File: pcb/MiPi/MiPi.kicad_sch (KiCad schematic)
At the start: 35 parts, among them J3 USB_C_Receptacle_USB2.0_14P, SW1 SW_Push, SW2 SW_Push, U1 RP2350_60QFN, U6 NCP1117-3.3_SOT223, Y1 Crystal_GND24

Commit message: Routed the analog switch and audio amp and audio jack
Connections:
- net REG_VIN is gone; now on net +5V: C38.1, U6.3 (VI)
- net GP20: now reaches U1.32 (GPIO20)
- net GP21: now reaches U1.33 (GPIO21)
- net GP22: now reaches U1.34 (GPIO22)
- net GP23: now reaches U1.35 (GPIO23)
- net GP24: now reaches U1.36 (GPIO24)
- net GP25: now reaches U1.37 (GPIO25)

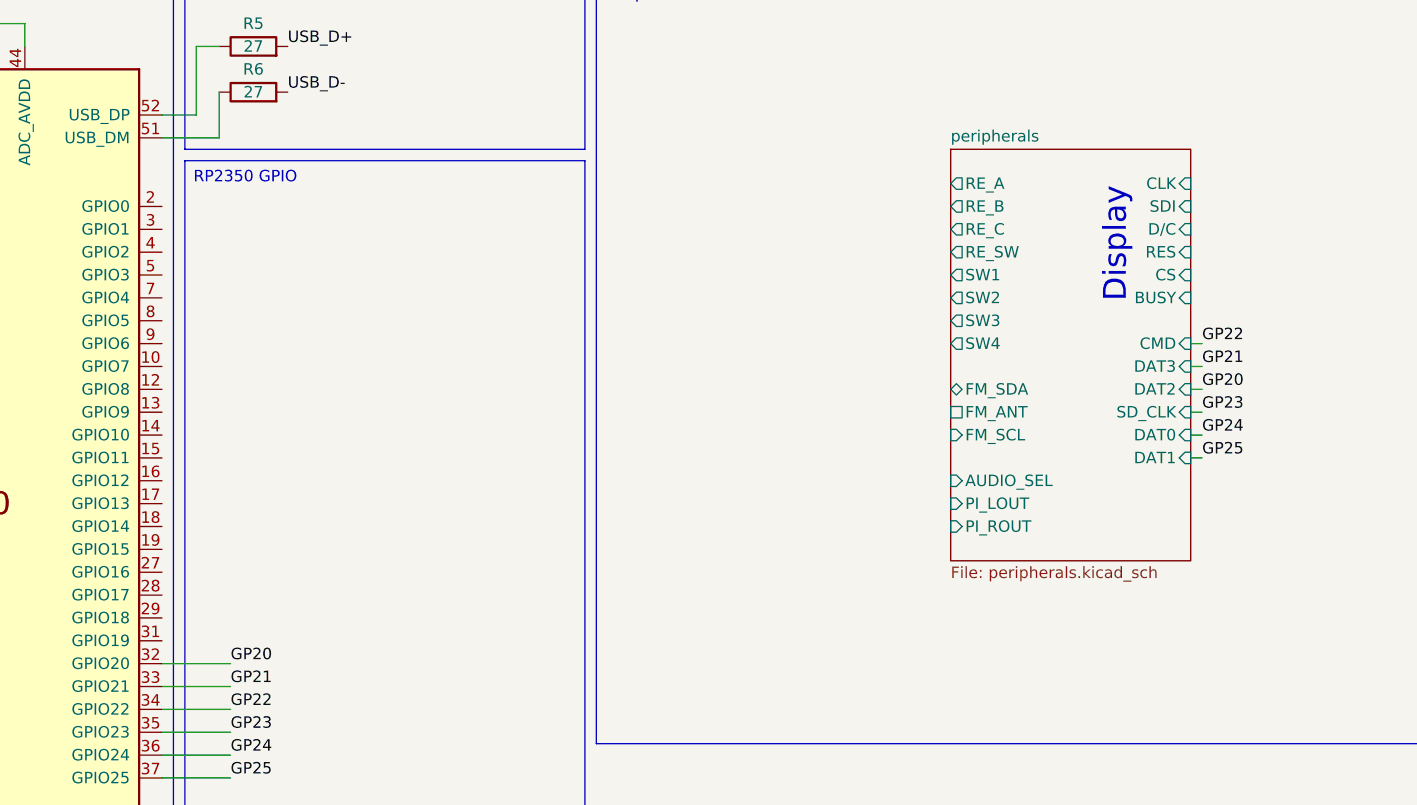
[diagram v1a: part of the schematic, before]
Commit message: Done the PCB layout
Remaining ground planes and power routing
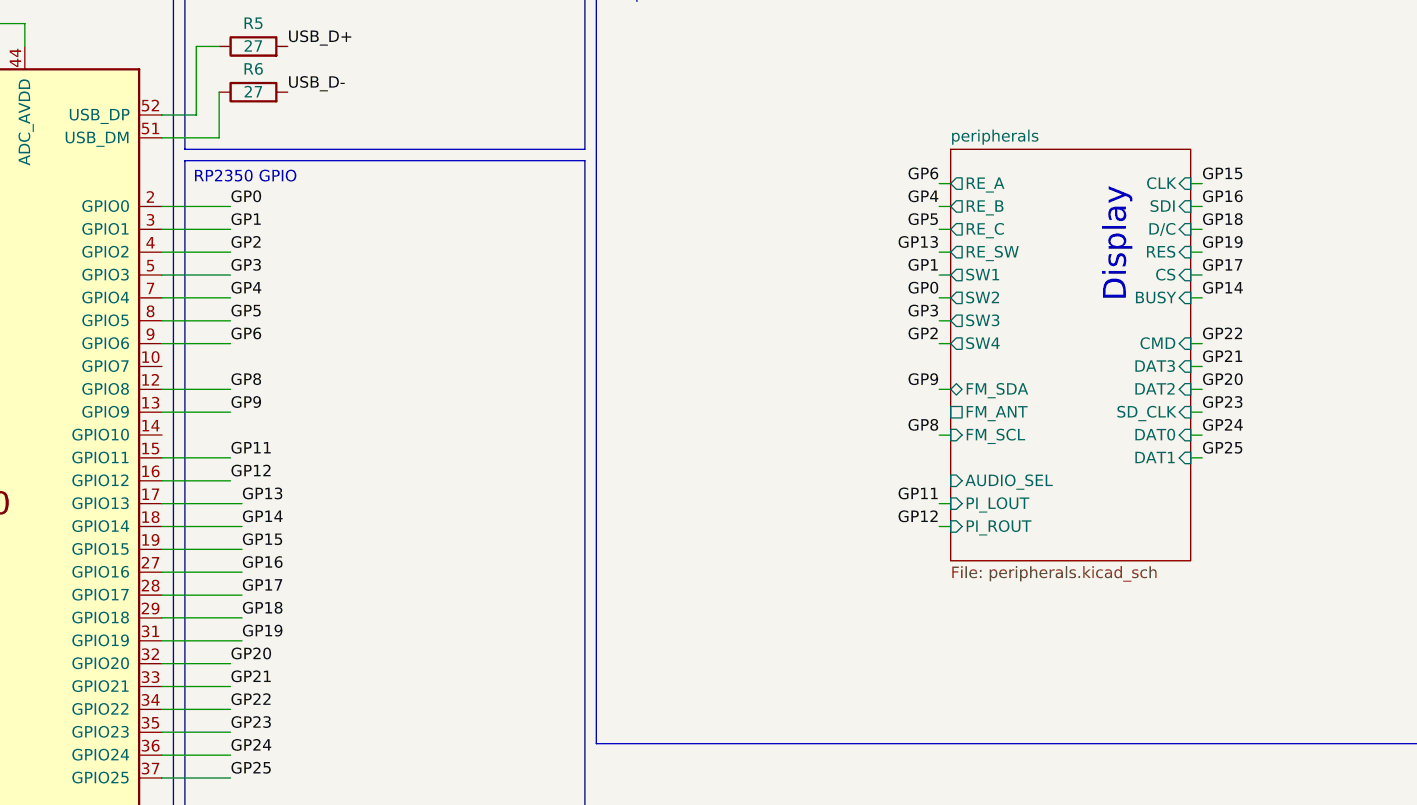
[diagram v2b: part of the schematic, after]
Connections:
- net GP8: now reaches U1.12 (GPIO8)
- net GP9: now reaches U1.13 (GPIO9)
- net GP11: now reaches U1.15 (GPIO11)
- net GP12: now reaches U1.16 (GPIO12)
- net GP13: now reaches U1.17 (GPIO13)
- net GP14: now reaches U1.18 (GPIO14)
- net GP15: now reaches U1.19 (GPIO15)
- net GP0: now reaches U1.2 (GPIO0)
- net GP16: now reaches U1.27 (GPIO16)
- net GP17: now reaches U1.28 (GPIO17)
- net GP18: now reaches U1.29 (GPIO18)
- net GP1: now reaches U1.3 (GPIO1)
- net GP19: now reaches U1.31 (GPIO19)
- net GP2: now reaches U1.4 (GPIO2)
- net GP3: now reaches U1.5 (GPIO3)
- net GP4: now reaches U1.7 (GPIO4)
- net GP5: now reaches U1.8 (GPIO5)
- net GP6: now reaches U1.9 (GPIO6)

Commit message: Made the Gerbers, BOM, and CDL for the first version of miPi
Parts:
- C1, C10, C11, C13, C2, C3, C4, C5, C6, C7, C8, C9: LCSC (none) -> C1525
- C12, C14, C15, C16: LCSC (none) -> C23733
- C17, C18: LCSC (none) -> C86285
- C38, C39: LCSC (none) -> C15525
- J3: LCSC (none) -> C5430474
- L1: LCSC (none) -> C42411119
- R1, R5, R6: LCSC (none) -> C1091
- R2, R3, R4: LCSC (none) -> C71623
- R28, R29: LCSC (none) -> C25941
- SW1, SW2: LCSC (none) -> C269272
- U1: LCSC (none) -> C41378174
- U6: LCSC (none) -> C26537
- Y1: LCSC (none) -> C20625731
